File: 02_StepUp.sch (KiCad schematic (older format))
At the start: 37 parts, among them J201 Conn_02x01, J301 Conn_02x04_Odd_Even, J302 Conn_02x04_Odd_Even, U201 XC6216C, U202 StepUp

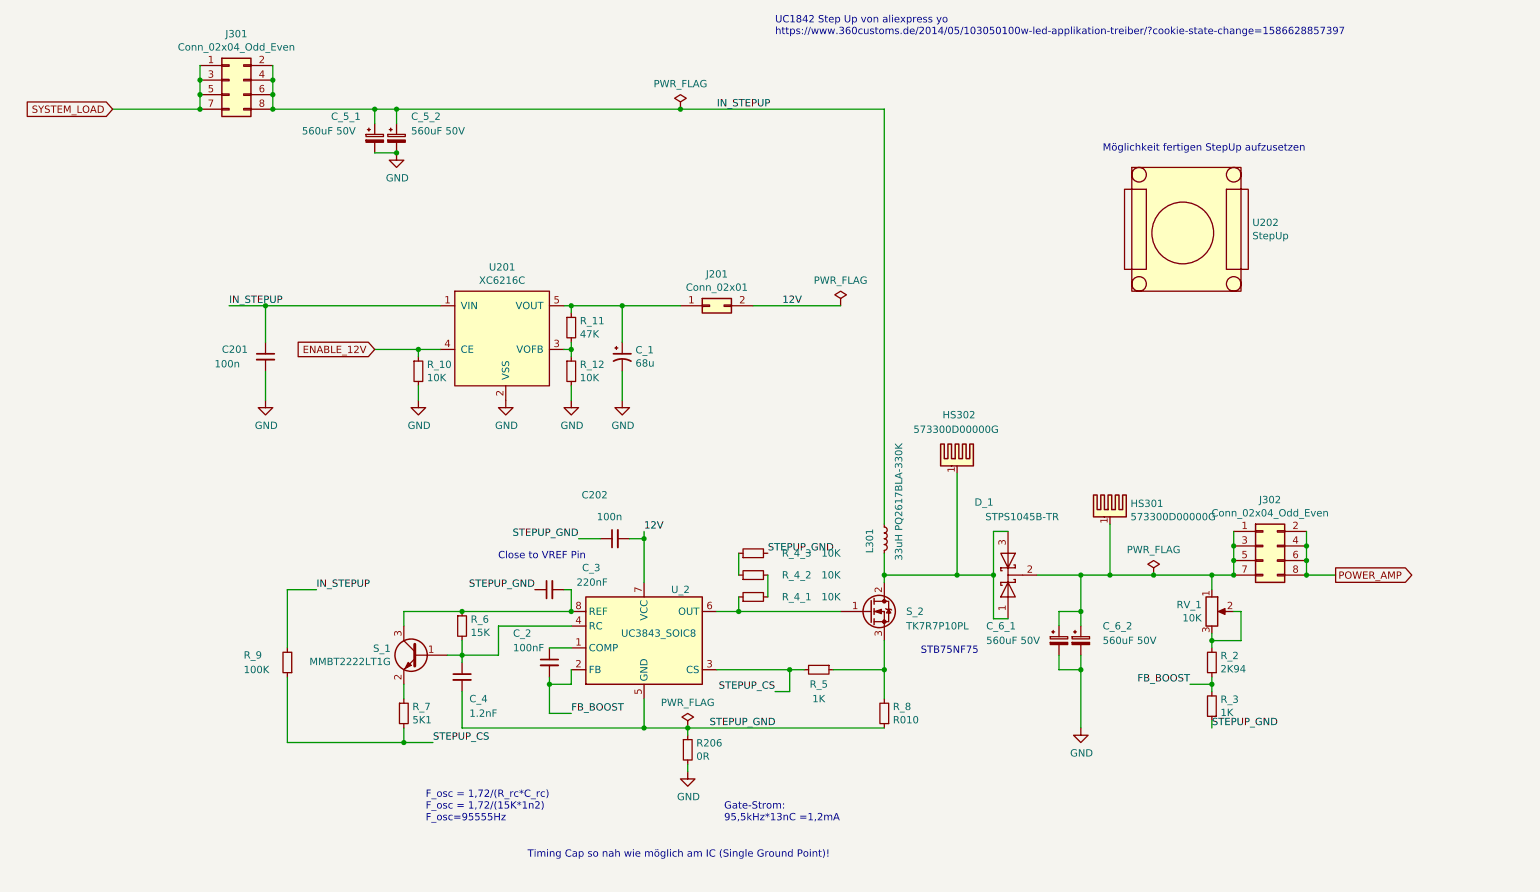
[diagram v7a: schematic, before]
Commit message: Charger austauschen gegen bq24610
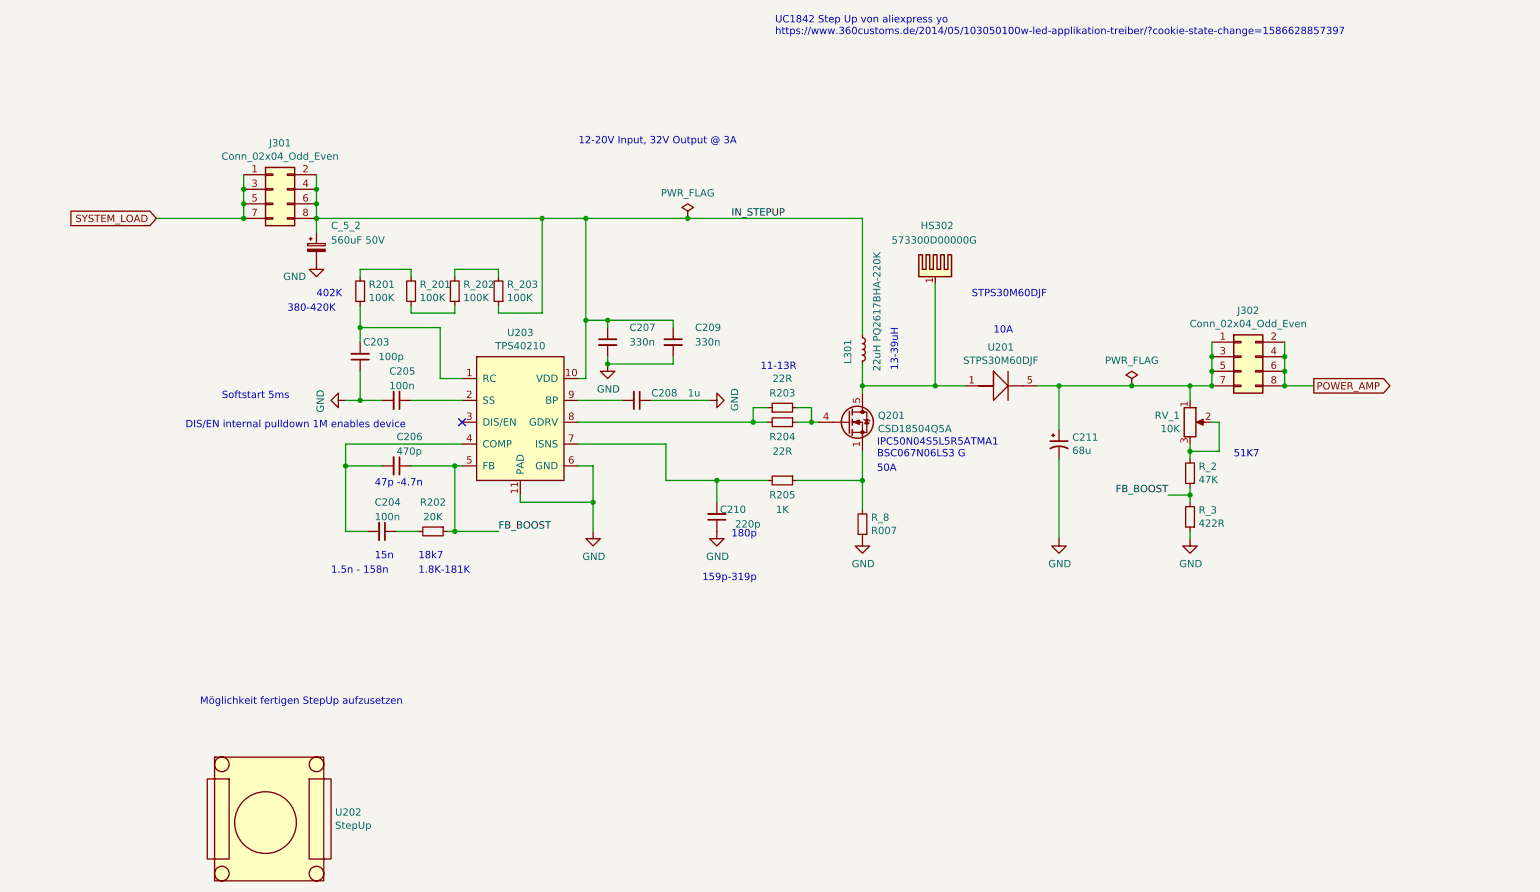
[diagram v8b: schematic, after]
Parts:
- removed C201, C202: 100n, Capacitor_SMD:C_0603_1608Metric_Pad1.05x0.95mm_HandSolder, symbol Device:C_Small
- removed C_1: 68u, Capacitor_THT:CP_Radial_D6.3mm_P2.50mm, symbol Device:CP1_Small
- removed C_2: 100nF, Capacitor_SMD:C_0603_1608Metric_Pad1.05x0.95mm_HandSolder, symbol Device:C_Small
- removed C_3: 220nF, Capacitor_SMD:C_0603_1608Metric_Pad1.05x0.95mm_HandSolder, symbol Device:C_Small
- removed C_4: 1.2nF, Capacitor_SMD:C_0603_1608Metric_Pad1.05x0.95mm_HandSolder, symbol Device:C_Small
- removed C_5_1, C_6_1, C_6_2: 560uF 50V, Capacitor_THT:CP_Radial_D12.5mm_P5.00mm, symbol Device:CP_Small
- removed D_1: STPS1045B-TR, Package_TO_SOT_SMD:TO-252-2, symbol Device:D_Schottky_x2_KCom_AKA
- removed HS301: 573300D00000G, Heatsink:Heatsink_AAVID_573300D00010G_TO-263, symbol Mechanical:Heatsink_Pad
- removed J201: Conn_02x01, Connector_PinHeader_2.54mm:PinHeader_1x02_P2.54mm_Vertical, symbol Connector_Generic:Conn_02x01
- removed R206: 0R, Resistor_SMD:R_1206_3216Metric_Pad1.42x1.75mm_HandSolder, symbol Device:R_Small
- removed R_10, R_12, R_4_1, R_4_2, R_4_3: 10K, Resistor_SMD:R_0603_1608Metric_Pad1.05x0.95mm_HandSolder, symbol Device:R_Small
- removed R_11: 47K, Resistor_SMD:R_0603_1608Metric_Pad1.05x0.95mm_HandSolder, symbol Device:R_Small
- removed R_5: 1K, Resistor_SMD:R_0603_1608Metric_Pad1.05x0.95mm_HandSolder, symbol Device:R_Small
- removed R_6: 15K, Resistor_SMD:R_0603_1608Metric_Pad1.05x0.95mm_HandSolder, symbol Device:R_Small
- removed R_7: 5K1, Resistor_SMD:R_0603_1608Metric_Pad1.05x0.95mm_HandSolder, symbol Device:R_Small
- removed R_9: 100K, Resistor_SMD:R_0603_1608Metric_Pad1.05x0.95mm_HandSolder, symbol Device:R_Small
- removed S_1: MMBT2222LT1G, Package_TO_SOT_SMD:SOT-23, symbol Device:Q_NPN_BEC
- removed S_2: TK7R7P10PL, Package_TO_SOT_SMD:TO-252-2, symbol Device:Q_NMOS_GDS
- removed U201: XC6216C, Package_TO_SOT_SMD:SOT-23-5_HandSoldering, symbol MukkeBox-rescue:XC6216C-Regulator_Linear
- removed U_2: UC3843_SOIC8, Package_SO:SOIC-8_3.9x4.9mm_P1.27mm, symbol MukkeBox-rescue:UC3843_SOIC8-Regulator_Controller
- added C203: 100p, Capacitor_SMD:C_0603_1608Metric_Pad1.05x0.95mm_HandSolder, symbol Device:C_Small
- added C204, C205: 100n, Capacitor_SMD:C_0603_1608Metric_Pad1.05x0.95mm_HandSolder, symbol Device:C_Small
- added C206: 470p, Capacitor_SMD:C_0603_1608Metric_Pad1.05x0.95mm_HandSolder, symbol Device:C_Small
- added C207, C209: 330n, Capacitor_SMD:C_1206_3216Metric, symbol Device:C_Small
- added C208: 1u, Capacitor_SMD:C_0603_1608Metric_Pad1.05x0.95mm_HandSolder, symbol Device:C_Small
- added C210: 220p, Capacitor_SMD:C_0603_1608Metric_Pad1.05x0.95mm_HandSolder, symbol Device:C_Small
- added C211: 68u, Capacitor_THT:CP_Radial_D5.0mm_P2.50mm, symbol Device:CP1_Small
- added Q201: CSD18504Q5A, Package_TO_SOT_SMD:TDSON-8-1_HandSoldering, symbol Transistor_FET:CSD18504Q5A
- added R201, R_201, R_202, R_203: 100K, Resistor_SMD:R_0603_1608Metric, symbol Device:R_Small
- added R202: 20K, Resistor_SMD:R_0603_1608Metric_Pad1.05x0.95mm_HandSolder, symbol Device:R_Small
- added R203, R204: 22R, Resistor_SMD:R_0603_1608Metric_Pad1.05x0.95mm_HandSolder, symbol Device:R_Small
- added R205: 1K, Resistor_SMD:R_0603_1608Metric_Pad1.05x0.95mm_HandSolder, symbol Device:R_Small
- added U201: STPS30M60DJF, Package_TO_SOT_SMD:TDSON-8-1_HandSoldering, symbol MukkeBox-rescue:Diode-TDSON-8-MySymbols
- added U203: TPS40210, Package_SO:MSOP-10-1EP_3x3mm_P0.5mm_EP1.68x1.88mm, symbol MukkeBox-rescue:TPS40210-MySymbols
- L301: value 33uH PQ2617BLA-330K -> 22uH PQ2617BHA-220K
- R_2: value 2K94 -> 47K
- R_3: value 1K -> 422R
- R_8: value R010 -> R007; footprint Resistor_SMD:R_1206_3216Metric_Pad1.42x1.75mm_HandSolder -> Resistor_SMD:R_2010_5025Metric_Pad1.52x2.65mm_HandSolder
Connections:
- net STEPUP_GND is gone; now on net GND: R_3.1, R_8.1
- net FB_BOOST: now also C206.1, R202.1, U203.5 (FB)
- net GND: now also C203.1, C205.2, C207.2, C208.1, C209.2, C210.1, C211.2, U203.11 (PAD), U203.6 (GND)
- net IN_STEPUP: now also C207.1, C209.1, R_203.1, U203.10 (VDD)
- net at R_8.2: now also Q201.1 (S), Q201.2 (S), Q201.3 (S), R205.1
- net at HS302.1, L301.2: now also Q201.5 (D), U201.1, U201.2 (Anode), U201.3 (Anode), U201.4 (Anode)
- net at J302.1 (Pin_1), J302.3 (Pin_3), J302.5 (Pin_5)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: now also C211.1, U201.5
- new net: Q201.4 (G), R203.2, R204.1
- new net: C203.2, R201.1, U203.1 (RC)
- new net: C205.1, U203.2 (SS)
- new net: C204.2, C206.2, U203.4 (COMP)
- new net: C210.2, R205.2, U203.7 (ISNS)
- new net: R203.1, R204.2, U203.8 (GDRV)
- new net: C208.2, U203.9 (BP)
- new net: C204.1, R202.2
- new net: R_201.1, R_202.1
- new net: R201.2, R_201.2
- new net: R_202.2, R_203.2
- no-connect marks 0 -> 1
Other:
- note added: "1.5n - 158n"
- note added: "1.8K-181K"
- note added: "10A"
- note added: "11-13R"
- note added: "12-20V Input, 32V Output @ 3A"
- note added: "13-39uH"
- note added: "159p-319p"
- note added: "15n"
- note added: "180p"
- note added: "18k7"
- note added: "380-420K"
- note added: "402K"
- note added: "47p -4.7n"
- note added: "50A"
- note added: "51K7"
- note added: "DIS/EN internal pulldown 1M enables device"
- note added: "IPC50N04S5L5R5ATMA1\nBSC067N06LS3 G"
- note added: "STPS30M60DJF"
- note added: "Softstart 5ms"
- note removed: "Close to VREF Pin"
- note removed: "F_osc = 1,72/(R_rc*C_rc)\nF_osc = 1,72/(15K*1n2)\nF_osc=95555Hz"
- note removed: "Gate-Strom:\n95,5kHz*13nC =1,2mA"
- note removed: "STB75NF75"
- note removed: "Timing Cap so nah wie möglich am IC (Single Ground Point)!"
- moved on the sheet: C_5_2, HS302, J301, J302, L301, RV_1, R_2, R_3, R_8, U202
